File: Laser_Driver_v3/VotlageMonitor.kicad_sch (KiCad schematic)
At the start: 93 parts, among them Q11 MMBT3904, Q12 MMBT3904, Q13 MMBT3904, Q14 MMBT3904, Q15 MMBT3904, Q16 MMBT3904, Q17 MMBT3904, Q18 MMBT3904, Q19 MMBT3904, U22 MCP6002-xMC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

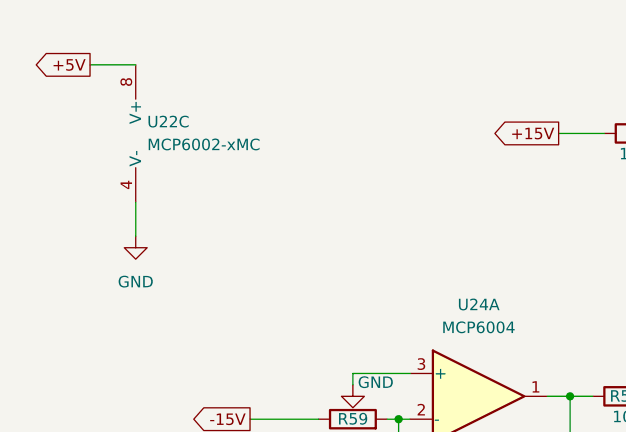
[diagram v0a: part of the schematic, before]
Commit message: Started placing voltage monitor parts.
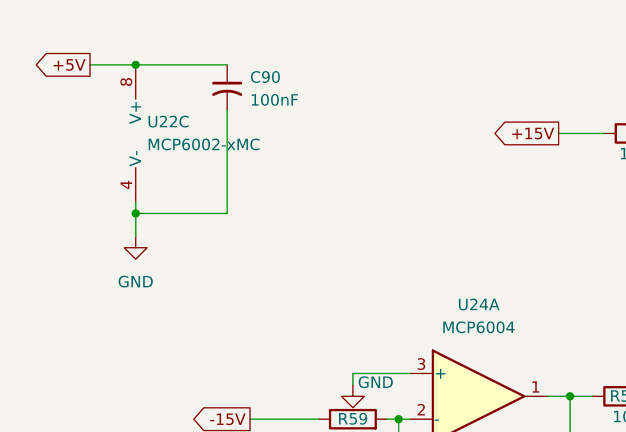
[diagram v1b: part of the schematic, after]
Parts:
- added C90: 100nF, Capacitor_SMD:C_0805_2012Metric_Pad1.18x1.45mm_HandSolder, symbol Device:C_Small_US
- C75, C76, C77, C78, C79, C80, C81, C82, C83, C84, C85, C86, C87, C88, C89: footprint (none) -> Capacitor_SMD:C_0805_2012Metric_Pad1.18x1.45mm_HandSolder
- U22: footprint Package_DFN_QFN:DFN-8-1EP_3x2mm_P0.5mm_EP1.75x1.45mm -> Package_SO:SOIC-8_3.9x4.9mm_P1.27mm
- U23, U24, U25, U26, U27, U28: footprint (none) -> Package_SO:SOIC-14_3.9x8.7mm_P1.27mm
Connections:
- net +5V: now also C90.1
- net GND: now also C90.2
